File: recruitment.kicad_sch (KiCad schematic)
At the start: 0 parts

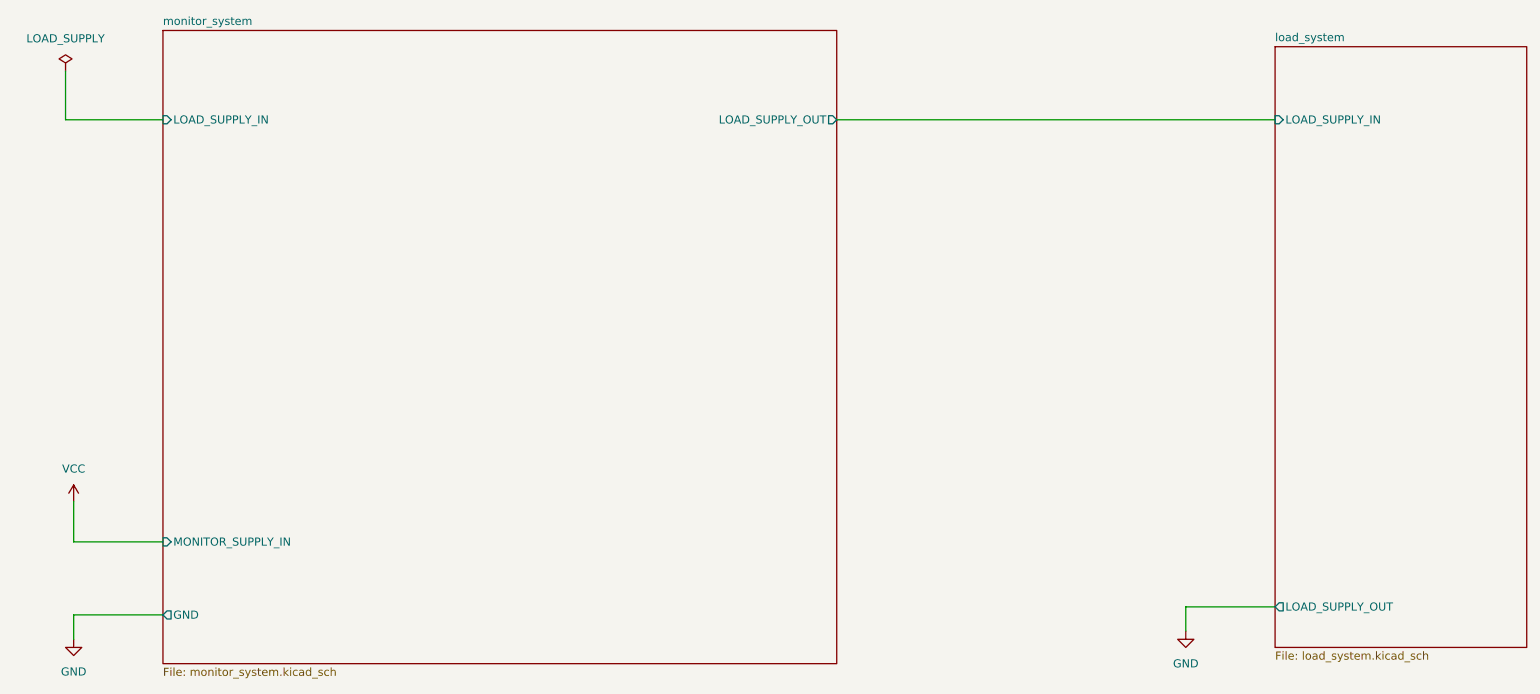
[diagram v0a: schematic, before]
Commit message: feat on the kicad schematic and the simulation folder
feat:added voltage Divider

feat:added ED555 ltSpice simulation

feat:added ED555 power cycle timer connection in kicad schematic

ERC:errors(1) warnings(3)
DRC:not tested
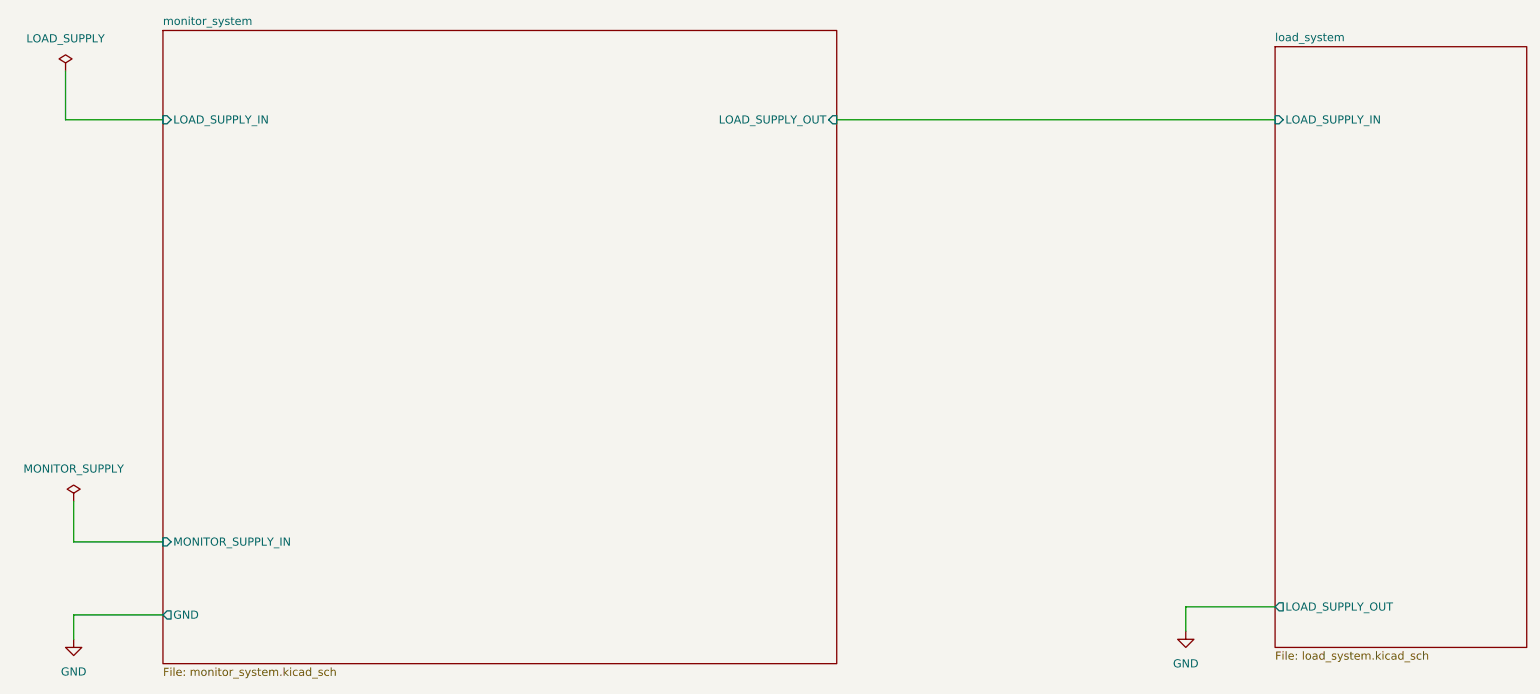
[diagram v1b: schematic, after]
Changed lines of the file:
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@@
+	)
+	(symbol
+		(lib_id "power:PWR_FLAG")
+		(at 38.1 128.27 0)
+		(unit 1)
+		(exclude_from_sim no)
+		(in_bom yes)
+		(on_board yes)
+		(dnp no)
+		(fields_autoplaced yes)
+		(property "Reference" "#FLG02"
+			(at 38.1 126.365 0)
+			(effects
+				(font
+					(size 1.27 1.27)
+				)
+				(hide yes)
+			)
+		)
+		(property "Value" "MONITOR_SUPPLY"
+			(at 38.1 123.19 0)
+			(effects
+				(font
+					(size 1.27 1.27)
+				)
+			)
+		)
+		(property "Footprint" ""
+			(at 38.1 128.27 0)
+			(effects
+				(font
+					(size 1.27 1.27)
+				)
+				(hide yes)
+			)
+		)
+		(property "Datasheet" "~"
+			(at 38.1 128.27 0)
+			(effects
+				(font
+					(size 1.27 1.27)
+				)
+				(hide yes)
+			)
+		)
+		(property "Description" "Special symbol for telling ERC where power comes from"
+			(at 38.1 128.27 0)
+			(effects
+				(font
+					(size 1.27 1.27)
+				)
+				(hide yes)
+			)
+		)
+		(pin "1"
+		)
+		(instances
+			(project "recruitment"
+				(path "/bdc7face-9f7c-4701-80bb-4cc144448db1"
+					(reference "#FLG02")
+					(unit 1)
+				)
+			)
+		)
 	)
 	(symbol
@@
 		)
 	)
-	(symbol
-		(lib_id "power:VCC")
-		(at 38.1 128.27 0)
-		(unit 1)
-		(exclude_from_sim no)
-		(in_bom yes)
-		(on_board yes)
-		(dnp no)
-		(fields_autoplaced yes)
-		(property "Reference" "#PWR01"
-			(at 38.1 132.08 0)
-			(effects
-				(font
-					(size 1.27 1.27)
-				)
-				(hide yes)
-			)
-		)
-		(property "Value" "VCC"
-			(at 38.1 123.19 0)
-			(effects
-				(font
-					(size 1.27 1.27)
-				)
-			)
-		)
-		(property "Footprint" ""
-			(at 38.1 128.27 0)
-			(effects
-				(font
-					(size 1.27 1.27)
-				)
-				(hide yes)
-			)
-		)
-		(property "Datasheet" ""
-			(at 38.1 128.27 0)
-			(effects
-				(font
-					(size 1.27 1.27)
-				)
-				(hide yes)
-			)
-		)
-		(property "Description" "Power symbol creates a global label with name \"VCC\""
-			(at 38.1 128.27 0)
-			(effects
-				(font
-					(size 1.27 1.27)
-				)
-				(hide yes)
-			)
-		)
-		(pin "1"
-		)
-		(instances
-			(project ""
-				(path "/bdc7face-9f7c-4701-80bb-4cc144448db1"
-					(reference "#PWR01")
-					(unit 1)
-				)
-			)
-		)
-	)
 	(sheet
 		(at 52.07 54.61)
@@
 			)
 		)
-		(pin "LOAD_SUPPLY_OUT" output
-			(at 157.48 68.58 0)
-			(effects
-				(font
-					(size 1.27 1.27)
-				)
-				(justify right)
-			)
-		)
 		(pin "GND" output
 			(at 52.07 146.05 180)
@@
 			)
 		)
+		(pin "LOAD_SUPPLY_OUT" input
+			(at 157.48 68.58 0)
+			(effects
+				(font
+					(size 1.27 1.27)
+				)
+				(justify right)
+			)
+		)
